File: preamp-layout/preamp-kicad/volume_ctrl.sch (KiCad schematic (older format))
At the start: 64 parts, among them J65 Conn_01x02_Male, J66 Conn_01x02_Male, J67 Conn_01x03_Female, J68 Conn_01x03_Female, J69 Conn_01x03_Male, J70 Conn_01x03_Male, J71 Conn_01x03_Male, J80 Conn_01x05_Male, U12 MCP4902, U13 MCP4902, U14 TL072, U15 TL072, U16 THAT2181, U17 THAT2181, U18 TL072, U19 THAT2181, U20 THAT2181, U21 TL072

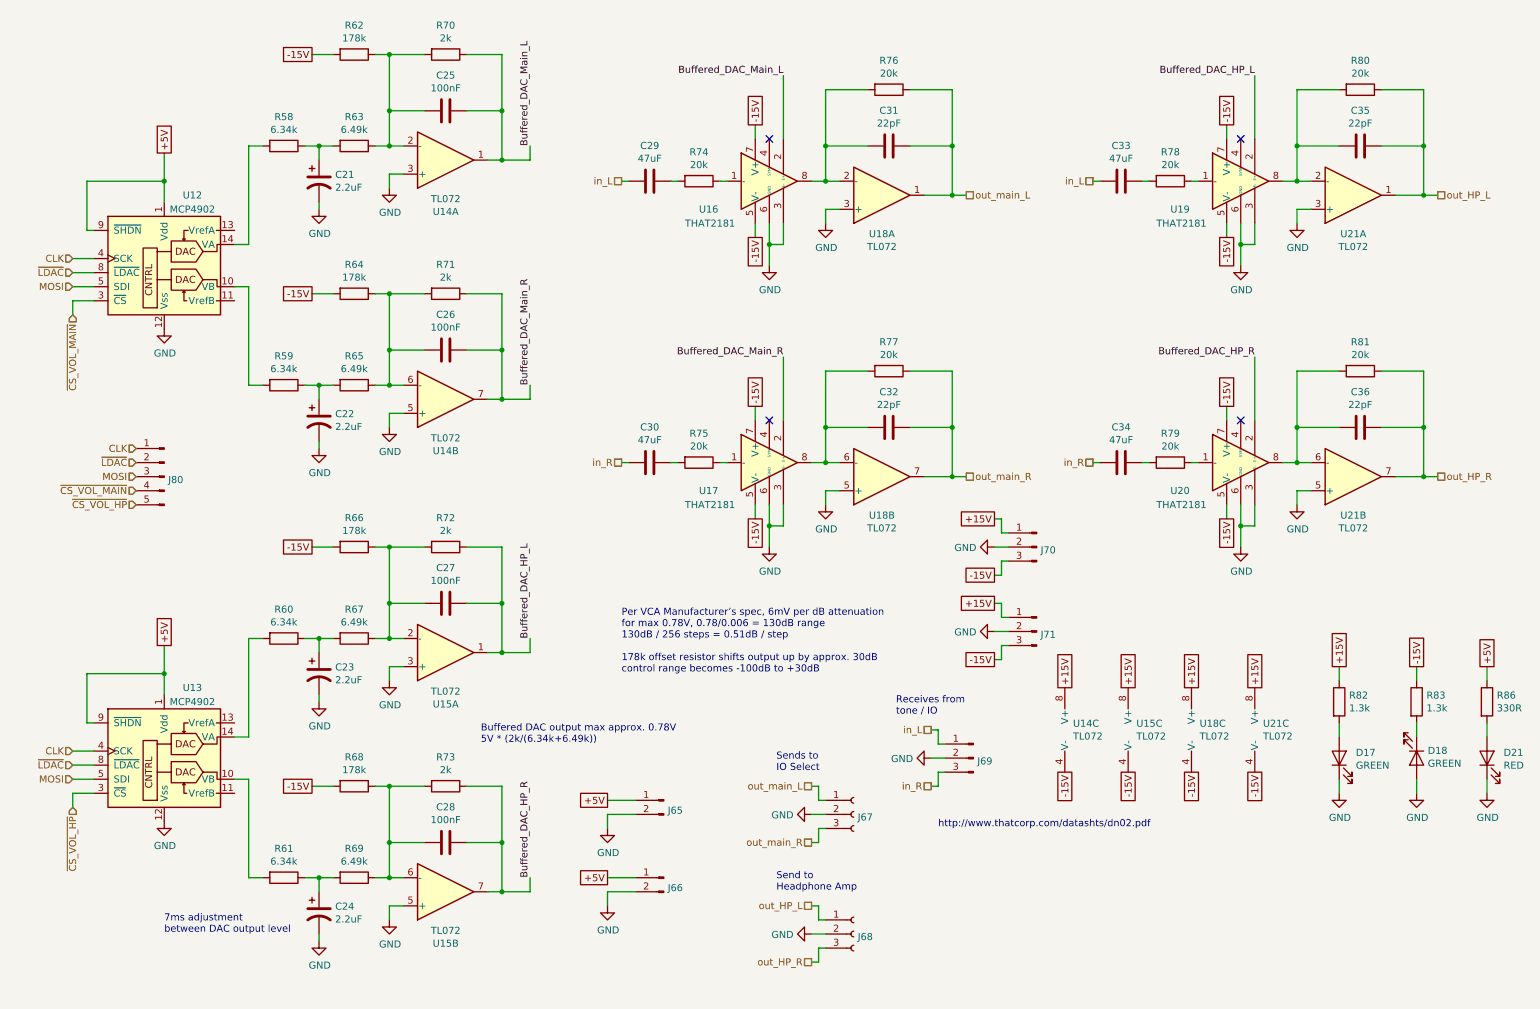
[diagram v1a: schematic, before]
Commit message: BOM Update
parts added to BOM, connector cleanup. Stopping point before renumbering refdes in a more intelligent way.
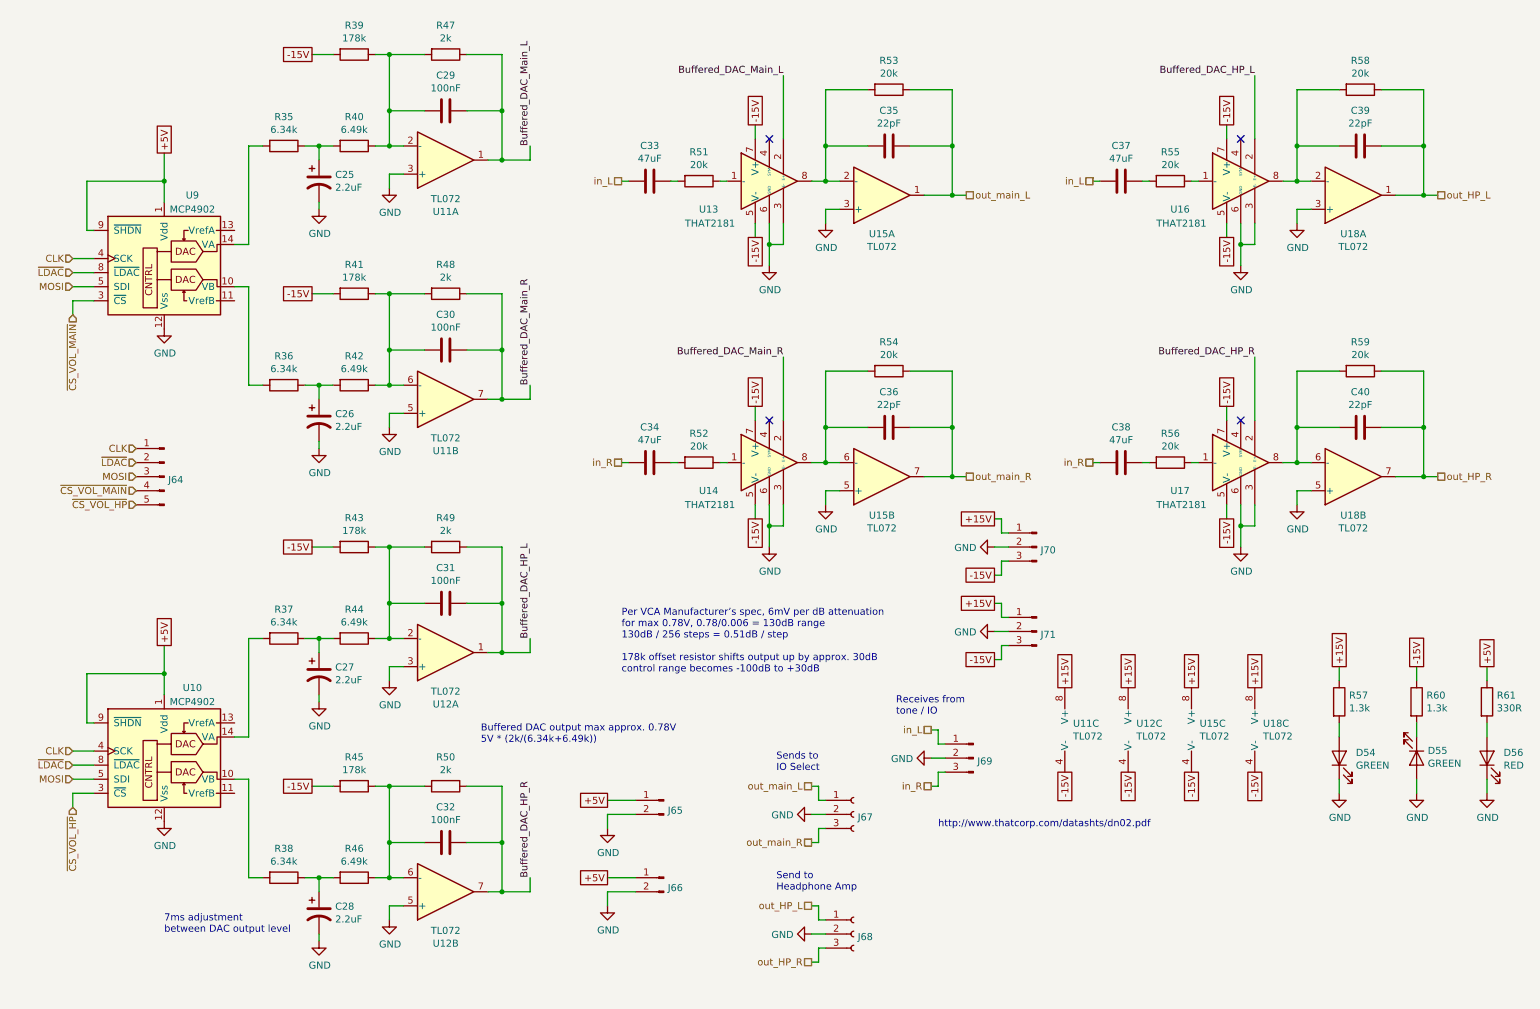
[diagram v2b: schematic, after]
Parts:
- renumbered C21 to C25, C22 to C26, C23 to C27, C24 to C28, C25 to C29, C26 to C30, C27 to C31, C28 to C32, C29 to C33, C30 to C34, C31 to C35, C32 to C36, C33 to C37, C34 to C38, C35 to C39, C36 to C40, D17 to D54, D18 to D55, D21 to D56, J80 to J64, R58 to R35, R59 to R36, R60 to R37, R61 to R38, R62 to R39, R63 to R40, R64 to R41, R65 to R42, R66 to R43, R67 to R44, R68 to R45, R69 to R46, R70 to R47, R71 to R48, R72 to R49, R73 to R50, R74 to R51, R75 to R52, R76 to R53, R77 to R54, R78 to R55, R79 to R56, R82 to R57, R80 to R58, R81 to R59, R83 to R60, R86 to R61, U13 to U10, U14 to U11, U15 to U12, U16 to U13, U17 to U14, U18 to U15, U19 to U16, U20 to U17, U21 to U18, U12 to U9

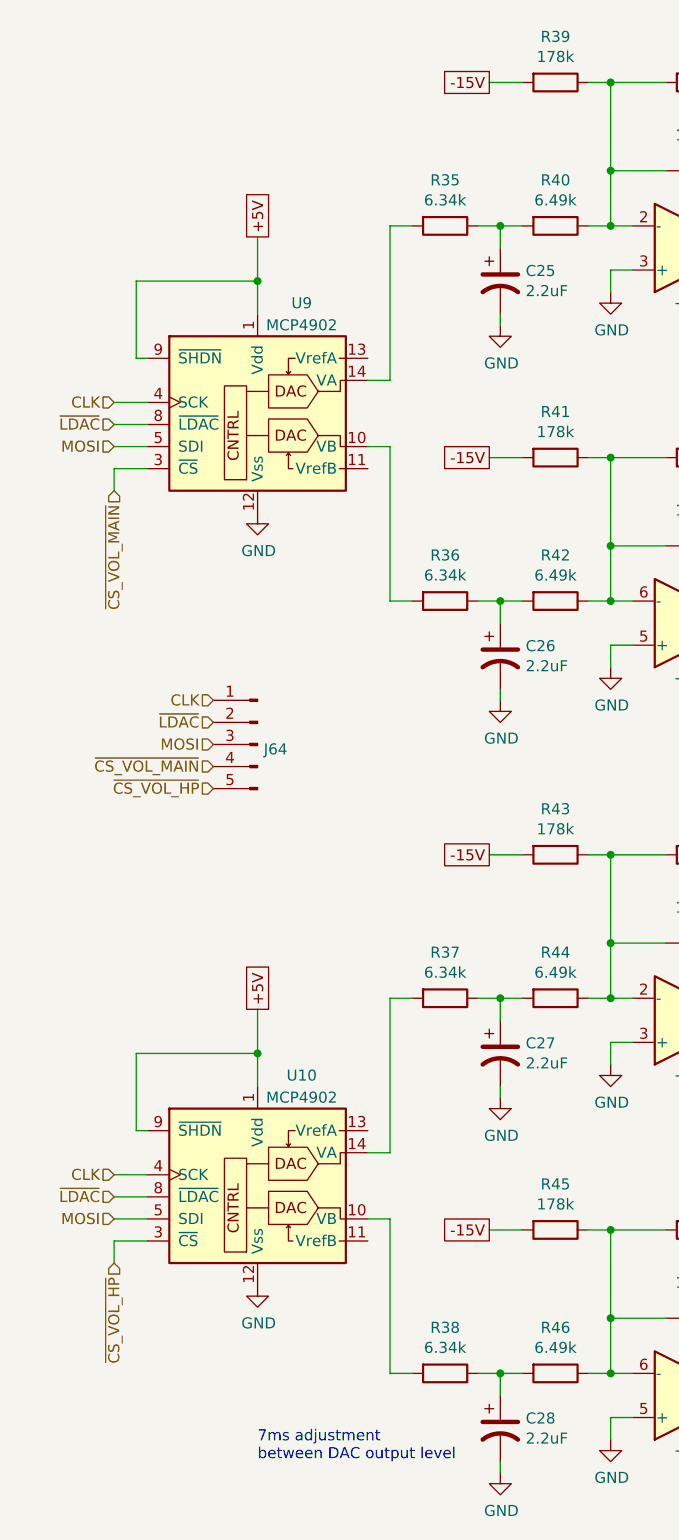
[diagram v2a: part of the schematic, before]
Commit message: Schematic Updates
Updated pin connections for DAC, footprint updates, MCU connections.
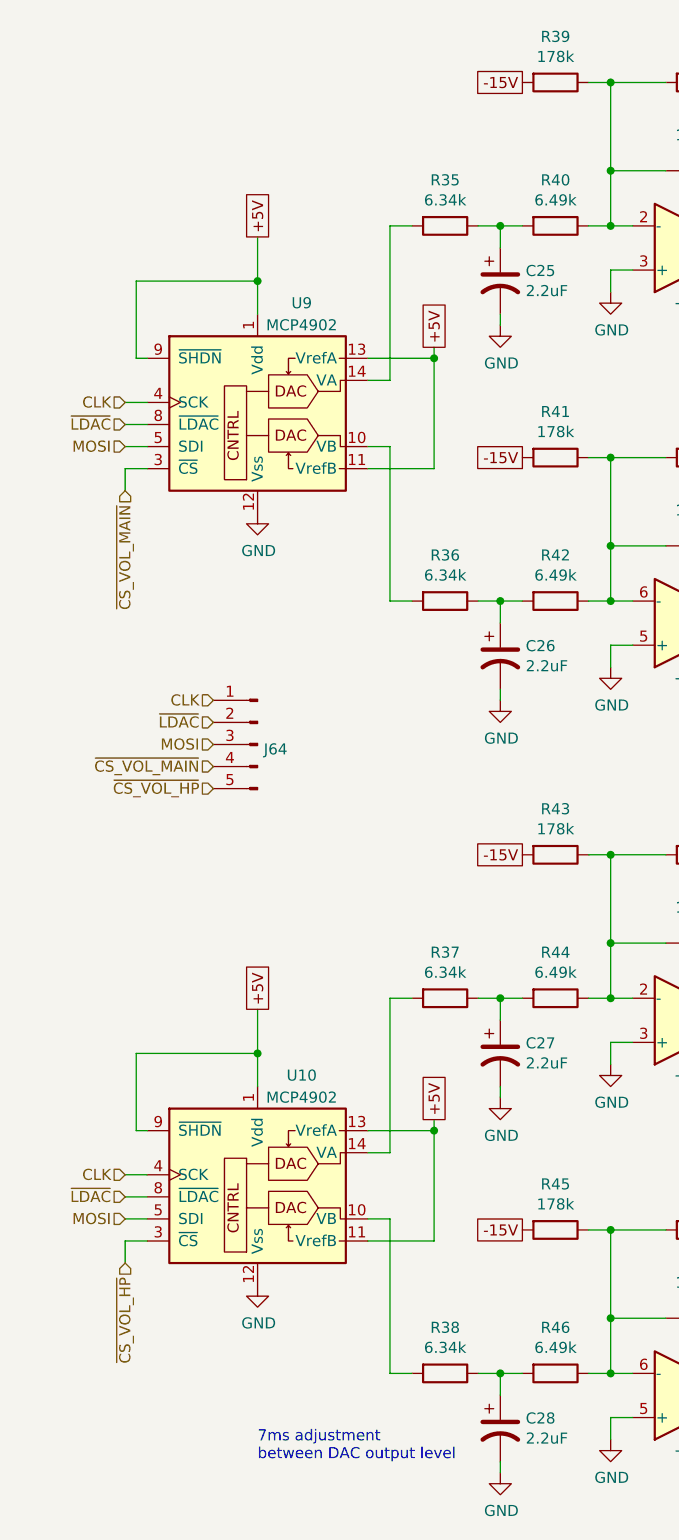
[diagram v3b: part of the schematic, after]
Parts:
- J64: footprint (none) -> Connector_PinHeader_2.54mm:PinHeader_1x05_P2.54mm_Vertical
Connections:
- net +5V: now also U10.11 (VrefB), U10.13 (VrefA), U9.11 (VrefB), U9.13 (VrefA)
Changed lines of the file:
@@
 	0    1    1    0
 $EndComp
-Text HLabel 850  6350 3    50   Input ~ 0
+Text HLabel 900  6350 3    50   Input ~ 0
 ~CS_VOL_HP
-Text HLabel 850  2650 0    50   Input ~ 0
-MOSI
-Text HLabel 850  2450 0    50   Input ~ 0
-CLK
-$Comp
-L Analog_DAC:MCP4902 U?
-U 1 1 6017A289
-P 1500 2450
-AR Path="/6017A289" Ref="U?"  Part="1"
-AR Path="/6009D432/6017A289" Ref="U9"  Part="1"
-F 0 "U9" H 1700 2900 50  0000 C CNN
-F 1 "MCP4902" H 1700 2800 50  0000 C CNN
-F 2 "" H 2300 2150 50  0001 C CNN
-F 3 "http://ww1.microchip.com/downloads/en/DeviceDoc/22250A.pdf" H 2300 2150 50  0001 C CNN
-	1    1500 2450
-	1    0    0    -1
-$EndComp
 $Comp
 L Device:R R?
@@
 	3000 1650 3100 1650
 Connection ~ 3100 1650
-Text GLabel 2550 1000 0    50   UnSpc ~ 0
+Text GLabel 2700 1000 0    50   UnSpc ~ 0
 -15V
-Wire Wire Line
-	2550 1000 2700 1000
 $Comp
 L Device:R R?
@@
 	3000 3350 3100 3350
 Connection ~ 3100 3350
-Text GLabel 2550 2700 0    50   UnSpc ~ 0
+Text GLabel 2700 2700 0    50   UnSpc ~ 0
 -15V
-Wire Wire Line
-	2550 2700 2700 2700
-Wire Wire Line
-	850  2450 1000 2450
-Wire Wire Line
-	850  2650 1000 2650
-Wire Wire Line
-	850  2750 1000 2750
 Text Label 4100 3350 1    50   ~ 0
 Buffered_DAC_Main_R
@@
 	0    1    1    0
 $EndComp
-Text HLabel 850  6150 0    50   Input ~ 0
+Text HLabel 900  6150 0    50   Input ~ 0
 MOSI
-Text HLabel 850  5950 0    50   Input ~ 0
+Text HLabel 900  5950 0    50   Input ~ 0
 CLK
 $Comp
@@
 	3000 5150 3100 5150
 Connection ~ 3100 5150
-Text GLabel 2550 4500 0    50   UnSpc ~ 0
+Text GLabel 2700 4500 0    50   UnSpc ~ 0
 -15V
-Wire Wire Line
-	2550 4500 2700 4500
 $Comp
 L Device:R R?
@@
 	3000 6850 3100 6850
 Connection ~ 3100 6850
-Text GLabel 2550 6200 0    50   UnSpc ~ 0
+Text GLabel 2700 6200 0    50   UnSpc ~ 0
 -15V
-Wire Wire Line
-	2550 6200 2700 6200
-Wire Wire Line
-	850  5950 1000 5950
-Wire Wire Line
-	850  6150 1000 6150
-Wire Wire Line
-	850  6250 1000 6250
 Text Label 4100 6850 1    50   ~ 0
 Buffered_DAC_HP_R
@@
 -15V
 Wire Wire Line
-	850  6250 850  6350
-Wire Wire Line
-	850  2750 850  2850
+	900  6250 900  6350
 Wire Wire Line
 	4100 5150 4100 5250
@@
 	3900 3450 4100 3450
 Wire Wire Line
-	2000 2350 2100 2350
-Wire Wire Line
-	2100 2350 2100 1650
-Wire Wire Line
 	2100 1650 2200 1650
-Wire Wire Line
-	2000 2650 2100 2650
-Wire Wire Line
-	2100 2650 2100 3350
 Wire Wire Line
 	2100 3350 2200 3350
@@
 $EndComp
 $Comp
-L power:GND #PWR069
-U 1 1 65235778
-P 1500 2950
-F 0 "#PWR069" H 1500 2700 50  0001 C CNN
-F 1 "GND" H 1505 2777 50  0000 C CNN
-F 2 "" H 1500 2950 50  0001 C CNN
-F 3 "" H 1500 2950 50  0001 C CNN
-	1    1500 2950
-	1    0    0    -1
-$EndComp
-$Comp
 L power:GND #PWR070
 U 1 1 65245F3B
@@
 	1    0    0    -1
 $EndComp
-Text HLabel 850  6050 0    50   Input ~ 0
+Text HLabel 900  6050 0    50   Input ~ 0
 ~LDAC
-Wire Wire Line
-	850  6050 1000 6050
-Text HLabel 850  2550 0    50   Input ~ 0
-~LDAC
-Wire Wire Line
-	850  2550 1000 2550
-Wire Wire Line
-	1000 2250 950  2250
-Wire Wire Line
-	950  2250 950  1900
 Wire Wire Line
 	1000 5750 950  5750
@@
 Text GLabel 1500 5200 1    50   UnSpc ~ 0
 +5V
-Wire Wire Line
-	950  1900 1500 1900
-Text GLabel 1500 1700 1    50   UnSpc ~ 0
-+5V
-Text HLabel 850  2850 3    50   Input ~ 0
-~CS_VOL_MAIN
 NoConn ~ 9150 3600
 NoConn ~ 9150 1600
@@
 	-1   0    0    -1
 $EndComp
-Connection ~ 1500 1900
-Wire Wire Line
-	1500 1900 1500 2050
-Wire Wire Line
-	1500 1700 1500 1900
 Connection ~ 1500 5400
 Wire Wire Line
@@
 F 0 "J64" H 1472 3978 50  0000 R CNN
 F 1 "Conn_01x05_Male" H 1608 4290 50  0001 C CNN
-F 2 "" H 1500 4000 50  0001 C CNN
+F 2 "Connector_PinHeader_2.54mm:PinHeader_1x05_P2.54mm_Vertical" H 1500 4000 50  0001 C CNN
 F 3 "~" H 1500 4000 50  0001 C CNN
 	1    1500 4000
@@
 Text HLabel 1300 4200 0    50   Input ~ 0
 ~CS_VOL_HP
+Text GLabel 2300 5700 1    50   UnSpc ~ 0
++5V
+Wire Wire Line
+	2300 5700 2300 5750
+Connection ~ 2300 5750
+Wire Wire Line
+	2300 5750 2300 6250
+Wire Wire Line
+	2000 5750 2300 5750
+Wire Wire Line
+	2000 6250 2300 6250
+Text GLabel 1500 1700 1    50   UnSpc ~ 0
++5V
+Wire Wire Line
+	1500 1700 1500 1900
+Wire Wire Line
+	1500 1900 1500 2050
+Connection ~ 1500 1900
+Text HLabel 900  2850 3    50   Input ~ 0
+~CS_VOL_MAIN
+Wire Wire Line
+	950  1900 1500 1900
+Wire Wire Line
+	950  2250 950  1900
+Wire Wire Line
+	1000 2250 950  2250
+Text HLabel 900  2550 0    50   Input ~ 0
+~LDAC
+$Comp
+L power:GND #PWR069
+U 1 1 65235778
+P 1500 2950
+F 0 "#PWR069" H 1500 2700 50  0001 C CNN
+F 1 "GND" H 1505 2777 50  0000 C CNN
+F 2 "" H 1500 2950 50  0001 C CNN
+F 3 "" H 1500 2950 50  0001 C CNN
+	1    1500 2950
+	1    0    0    -1
+$EndComp
+Wire Wire Line
+	900  2750 900  2850
+$Comp
+L Analog_DAC:MCP4902 U?
+U 1 1 6017A289
+P 1500 2450
+AR Path="/6017A289" Ref="U?"  Part="1"
+AR Path="/6009D432/6017A289" Ref="U9"  Part="1"
+F 0 "U9" H 1700 2900 50  0000 C CNN
+F 1 "MCP4902" H 1700 2800 50  0000 C CNN
+F 2 "" H 2300 2150 50  0001 C CNN
+F 3 "http://ww1.microchip.com/downloads/en/DeviceDoc/22250A.pdf" H 2300 2150 50  0001 C CNN
+	1    1500 2450
+	1    0    0    -1
+$EndComp
+Text HLabel 900  2450 0    50   Input ~ 0
+CLK
+Text HLabel 900  2650 0    50   Input ~ 0
+MOSI
+Text GLabel 2300 2200 1    50   UnSpc ~ 0
++5V
+Wire Wire Line
+	2000 2750 2300 2750
+Wire Wire Line
+	2300 2250 2300 2750
+Wire Wire Line
+	2300 2200 2300 2250
+Connection ~ 2300 2250
+Wire Wire Line
+	2000 2250 2300 2250
+Wire Wire Line
+	2100 2650 2100 3350
+Wire Wire Line
+	2000 2650 2100 2650
+Wire Wire Line
+	2100 2350 2100 1650
+Wire Wire Line
+	2000 2350 2100 2350
+Wire Wire Line
+	900  5950 1000 5950
+Wire Wire Line
+	900  6050 1000 6050
+Wire Wire Line
+	900  6150 1000 6150
+Wire Wire Line
+	900  6250 1000 6250
+Wire Wire Line
+	900  2450 1000 2450
+Wire Wire Line
+	900  2550 1000 2550
+Wire Wire Line
+	1000 2650 900  2650
+Wire Wire Line
+	900  2750 1000 2750
 $EndSCHEMATC
